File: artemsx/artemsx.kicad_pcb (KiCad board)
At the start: 2 copper layers, 132 parts, among them J1 PS2_CONN, J2 MSX_Slot, J3 MSX_Slot, J4 CONN_JOY, J5 CONN_JOY, J6 PWR_conn, U1 74HC32, U10 TMS99x8, U11 74HCT244, U12 74HCT244, U13 74HCT245, U14 74HCT244, U15 74HC74, U16 74HC08, U17 74HC32, U18 Z84C00, U19 82C55A, U2 74HC04, U20 74HC153, U21 74HC139, U23 74HC138, U24 74HC32, U25 SST39SF0x0, U26 ATMEGA328P, U27 74HC154, U28 74HC595, U29 74HC595, U3 HM62256ALP-10, U30 74HC595, U31 74HC595, U32 74HC595, U33 74HC595, U34 74HC595, U35 74HC595, U36 74HC595, U37 74HC595, U38 4069, U39 74HC07, U4 HM62256ALP-10, U40 74HC74, U41 AY-3-8910, U42 74HC157, U43 74HC157, U44 74HC32, U45 74HC595, U5 74HCT04, U6 74HCT574, U7 74HCT574, U8 74HCT574, U9 HM62256ALP-10, Y1 10.7386Mhz, Y2 16Mhz, Y3 3.58Mhz

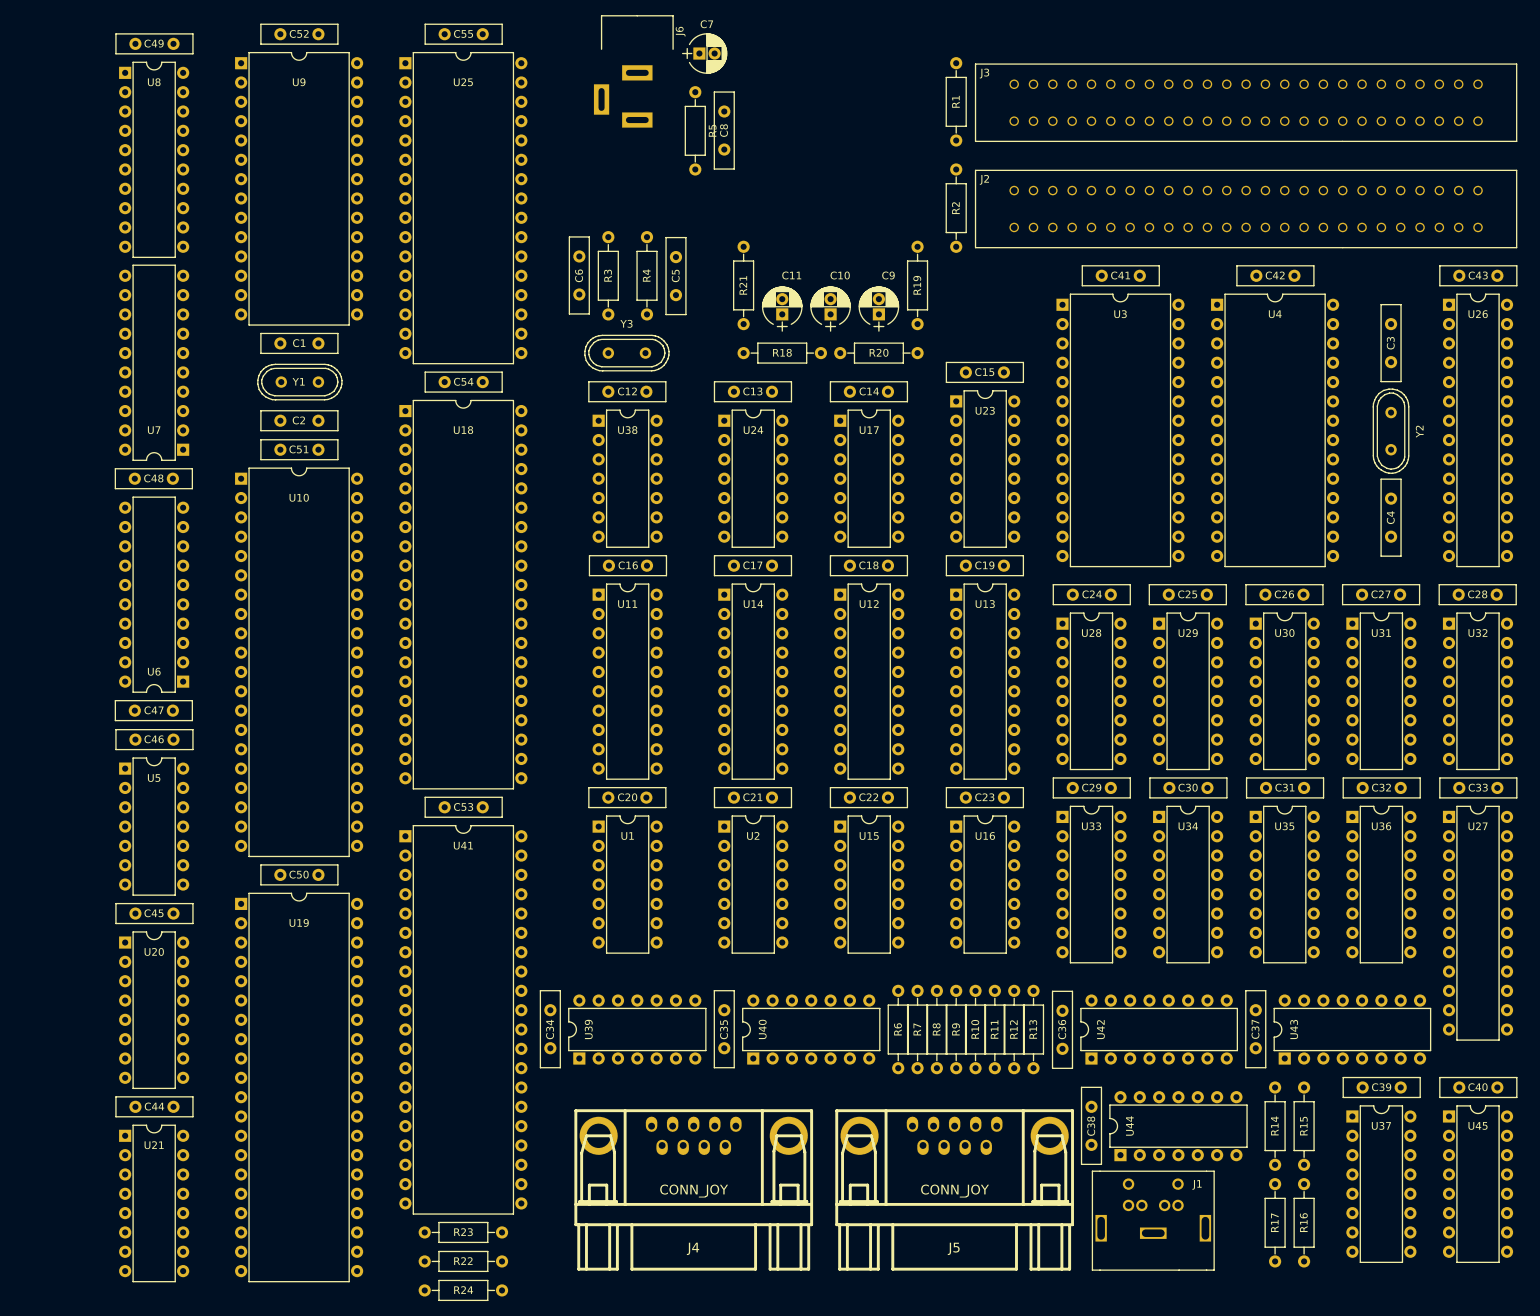
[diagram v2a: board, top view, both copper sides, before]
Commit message: Replace the footprint of the disc capacitors
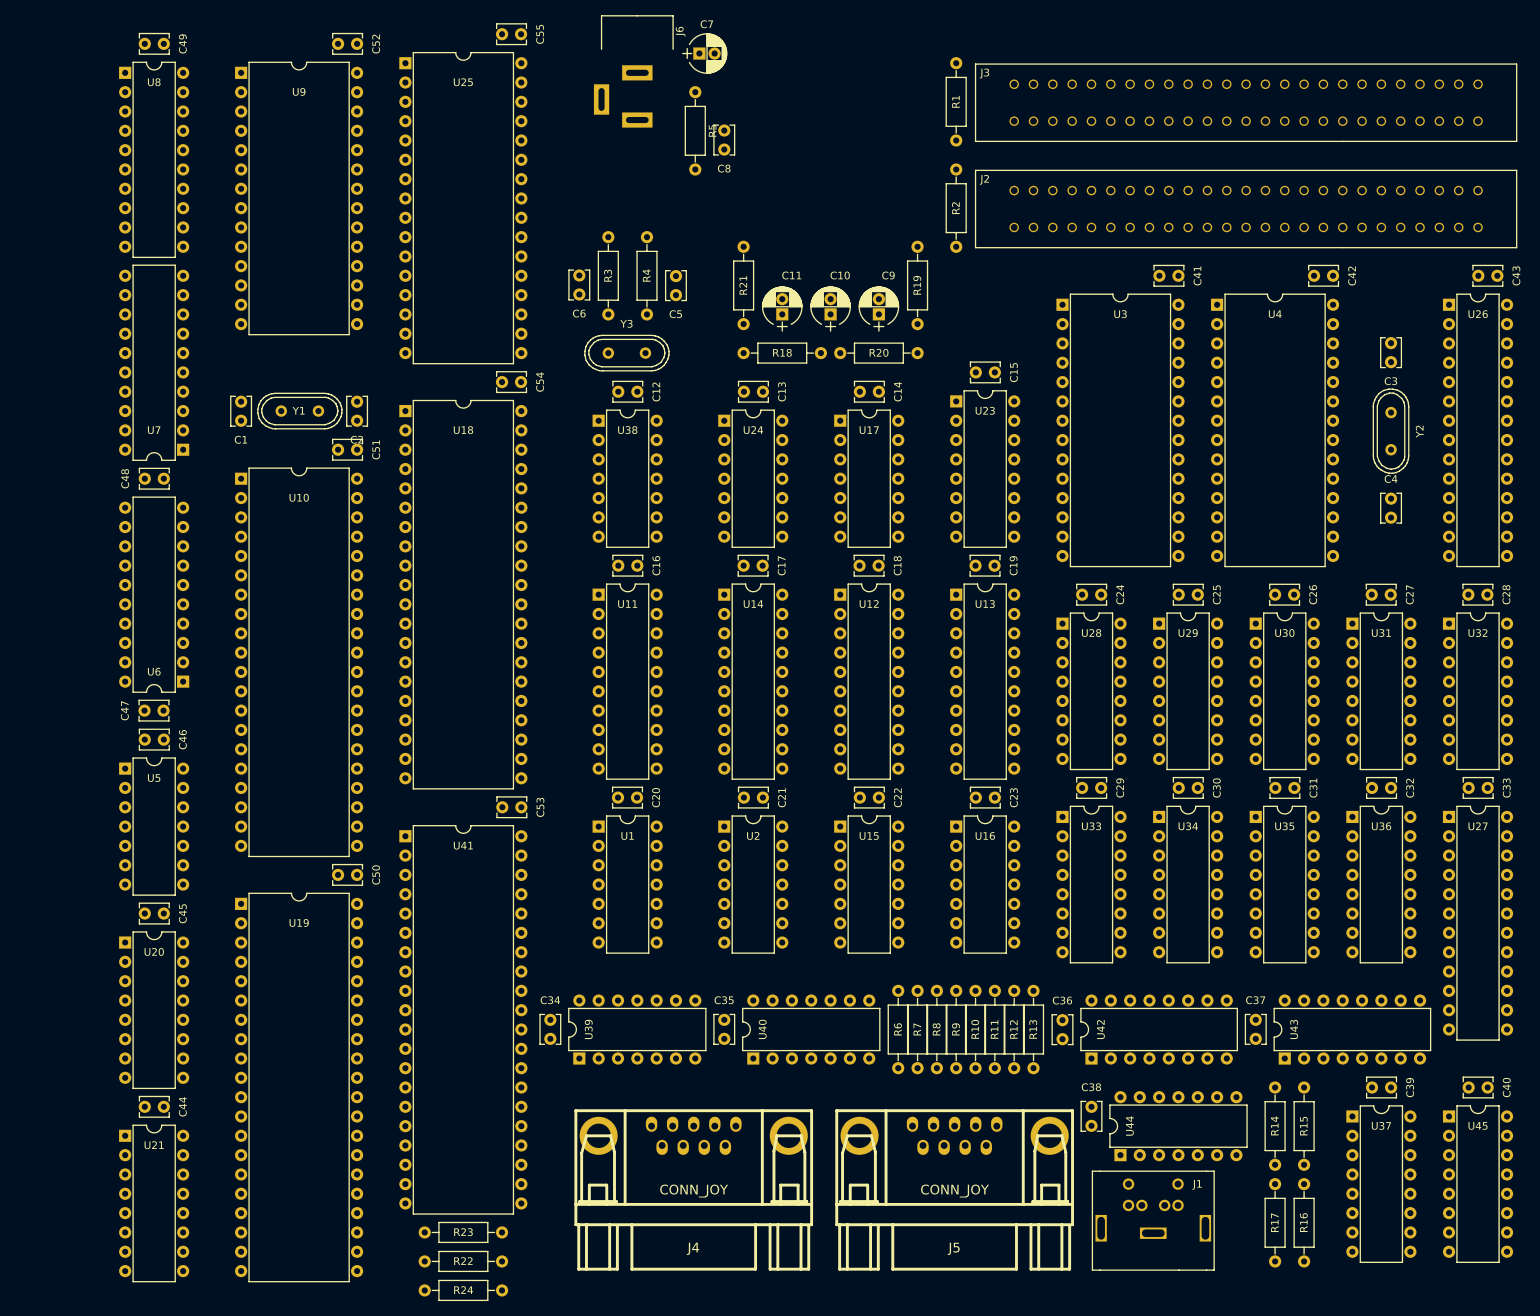
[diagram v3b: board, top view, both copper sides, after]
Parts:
- moved C1 11.4 mm to (123.2, 96.5), turned to 90 degrees
- moved C2 10.1 mm to (138.4, 96.5), turned to 90 degrees
- moved C52 5.24 mm to (138.4, 47.0)
- moved C50 5.08 mm to (138.4, 156.2)
- moved C51 5.08 mm to (138.4, 100.3)
- moved C53 5.08 mm to (160.0, 147.3)
- moved C41 5.08 mm to (246.4, 77.5)
- moved C42 5.08 mm to (266.7, 77.5)
- moved C54 5.04 mm to (160.0, 91.4)
- moved C55 5.04 mm to (160.0, 45.7)
- moved Y1 3.81 mm to (130.9, 95.2)
- moved C48 1.31 mm to (110.5, 104.1)
- moved C33 1.27 mm to (287.0, 144.8)
- moved C40 1.27 mm to (287.0, 184.2)
- moved C16 1.27 mm to (175.3, 115.6)
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
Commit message: Place the CAS elements in the PCB
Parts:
- added C56: 1uF, artemsx:Radial_capacitor, F.Cu at (165.6, 52.1)
- added C57: 22nF, artemsx:Disc_capacitor, F.Cu at (167.6, 58.4)
- added C58: 22nF, artemsx:Disc_capacitor, F.Cu at (207.0, 73.7)
- added C59: 1uF, artemsx:Radial_capacitor, F.Cu at (180.9, 66.0)
- added J7: Audio_conn, artemsx:Jack_conn, F.Cu at (185.3, 55.9)
- added J8: Audio_conn, artemsx:Jack_conn, F.Cu at (200.7, 55.8)
- added R25: 4k7, artemsx:Axial_resistor, F.Cu at (171.4, 59.7)
- added R26: 4k7, artemsx:Axial_resistor, F.Cu at (174.0, 49.5)
- added R27: 100, artemsx:Axial_resistor, F.Cu at (176.5, 59.7)
- added R28: 2k7, artemsx:Axial_resistor, F.Cu at (166.4, 64.8)
- added R29: 2k7, artemsx:Axial_resistor, F.Cu at (166.4, 67.3)
- added R30: 10k, artemsx:Axial_resistor, F.Cu at (196.8, 62.2)
- added R31: 4k7, artemsx:Axial_resistor, F.Cu at (186.7, 64.8)
- added R32: 220k, artemsx:Axial_resistor, F.Cu at (196.8, 67.3)
- added R33: 1k, artemsx:Axial_resistor, F.Cu at (186.7, 69.8)
- added R34: 10k, artemsx:Axial_resistor, F.Cu at (213.4, 57.1)
- added R35: 470k, artemsx:Axial_resistor, F.Cu at (210.8, 47.0)
- added U46: LM311, artemsx:DIP-8_300, F.Cu at (205.7, 68.6)
- moved J6 72.4 mm to (98.2, 55.6)
- moved C8 71.1 mm to (115.6, 62.1)
- moved C7 71.1 mm to (112.3, 49.5)
- moved R5 71.1 mm to (111.8, 54.6)
- moved U8 47.0 mm to (109.2, 97.8)
- moved C49 47.0 mm to (114.3, 94.0)
- moved C2 38.4 mm to (100.3, 101.6), turned to 180 degrees
- moved Y1 34.7 mm to (99.1, 109.1), turned to 90 degrees
- moved U7 34.5 mm to (95.2, 128.3), turned to 0 degrees
- moved C1 30.6 mm to (100.3, 116.8), turned to 180 degrees
- moved R24 29.0 mm to (129.5, 203.2)
- moved C46 27.5 mm to (97.8, 161.3), turned to 270 degrees
- moved U5 25.0 mm to (101.6, 166.4), turned to 90 degrees
- moved C45 23.4 mm to (95.2, 176.5), turned to 270 degrees
- moved C48 22.8 mm to (100.3, 124.5), turned to 180 degrees
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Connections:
- U19 pad 12: /PPI/CASOUT -> /CASOUT
- U41 pad 14: /PSG/IOA7 -> /CASIN

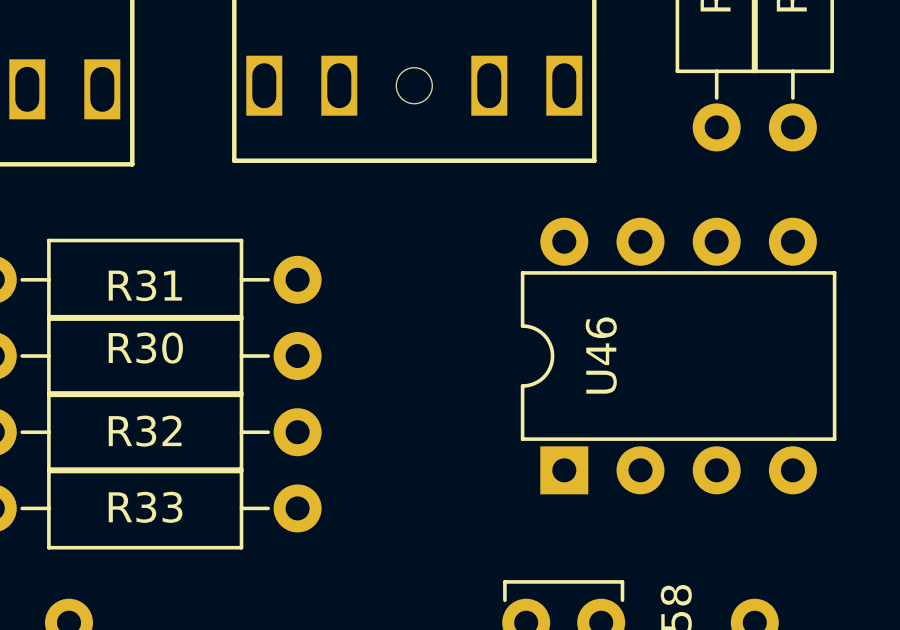
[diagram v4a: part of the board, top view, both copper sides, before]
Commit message: Add a decoupling capacitor for the LM311.
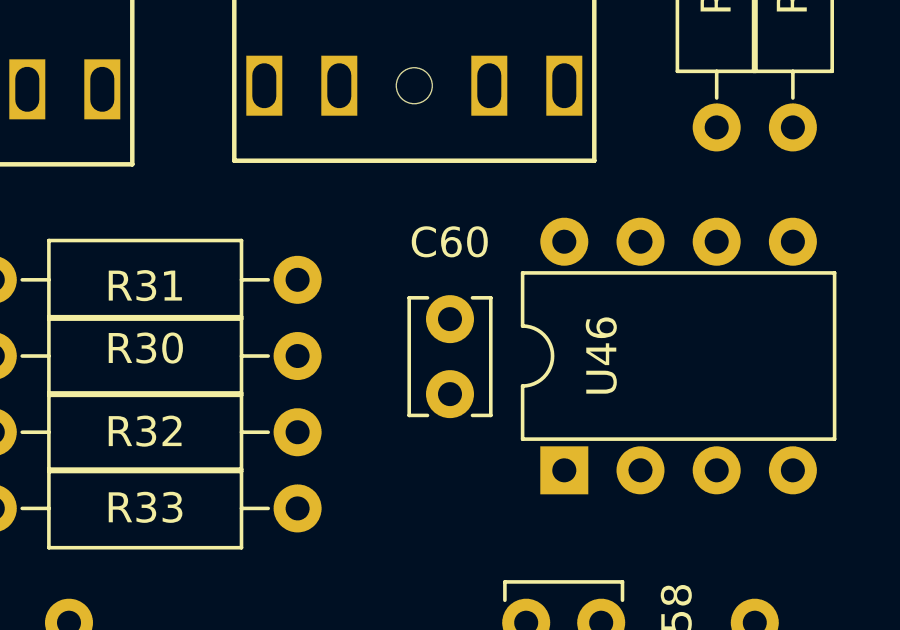
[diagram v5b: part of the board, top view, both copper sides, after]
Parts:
- added C60: 22pF, artemsx:Disc_capacitor, F.Cu at (201.9, 63.5)
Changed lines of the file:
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@@
 (kicad_pcb (version 4) (host pcbnew 4.0.7)
   (general
-    (links 896)
-    (no_connects 884)
-    (area 92.75 41.146666 291.905 210.11375)
+    (links 898)
+    (no_connects 898)
+    (area 0 0 0 0)
     (thickness 1.6)
     (drawings 0)
     (tracks 0)
     (zones 0)
-    (modules 150)
+    (modules 151)
     (nets 322)
   )
@@
       (rotate (xyz 0 0 0))
     )
+  )
+  (module artemsx:Disc_capacitor (layer F.Cu)
+    (at 201.93 63.54 270)
+    (descr "C, Disc series, Radial, pin pitch=2.50mm, , diameter*width=3.8*2.6mm^2, Capacitor, http://www.vishay.com/docs/45233/krseries.pdf")
+    (tags "C Disc series Radial pin pitch 2.50mm  diameter 3.8mm width 2.6mm Capacitor")
+    (fp_text reference C60 (at -2.54 0 360) (layer F.SilkS)
+      (effects (font (size 1 1) (thickness 0.15)))
+    )
+    (fp_text value 22pF (at 5.08 -1.27 450) (layer F.Fab)
+      (effects (font (size 1 1) (thickness 0.15)))
+    )
+    (fp_line (start -0.65 -1.3) (end -0.65 1.3) (layer F.Fab) (width 0.1))
+    (fp_line (start -0.65 1.3) (end 3.15 1.3) (layer F.Fab) (width 0.1))
+    (fp_line (start 3.15 1.3) (end 3.15 -1.3) (layer F.Fab) (width 0.1))
+    (fp_line (start 3.15 -1.3) (end -0.65 -1.3) (layer F.Fab) (width 0.1))
+    (fp_line (start -0.71 -1.36) (end 3.21 -1.36) (layer F.SilkS) (width 0.12))
+    (fp_line (start -0.71 1.36) (end 3.21 1.36) (layer F.SilkS) (width 0.12))
+    (fp_line (start -0.71 -1.36) (end -0.71 -0.75) (layer F.SilkS) (width 0.12))
+    (fp_line (start -0.71 0.75) (end -0.71 1.36) (layer F.SilkS) (width 0.12))
+    (fp_line (start 3.21 -1.36) (end 3.21 -0.75) (layer F.SilkS) (width 0.12))
+    (fp_line (start 3.21 0.75) (end 3.21 1.36) (layer F.SilkS) (width 0.12))
+    (fp_line (start -1.05 -1.65) (end -1.05 1.65) (layer F.CrtYd) (width 0.05))
+    (fp_line (start -1.05 1.65) (end 3.55 1.65) (layer F.CrtYd) (width 0.05))
+    (fp_line (start 3.55 1.65) (end 3.55 -1.65) (layer F.CrtYd) (width 0.05))
+    (fp_line (start 3.55 -1.65) (end -1.05 -1.65) (layer F.CrtYd) (width 0.05))
+    (fp_text user %R (at -2.54 0 360) (layer F.Fab)
+      (effects (font (size 1 1) (thickness 0.15)))
+    )
+    (pad 1 thru_hole circle (at 0 0 270) (size 1.6 1.6) (drill 0.8) (layers *.Cu *.Mask)
+      (net 18 VCC))
+    (pad 2 thru_hole circle (at 2.5 0 270) (size 1.6 1.6) (drill 0.8) (layers *.Cu *.Mask)
+      (net 2 GND))
+    (model ${KIPRJMOD}/artemsx.3dshapes/Disc_capacitor.wrl
+      (at (xyz 0 0 0))
+      (scale (xyz 1 0.5 1))
+      (rotate (xyz 0 0 0))
+    )
